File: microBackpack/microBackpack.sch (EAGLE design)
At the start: 93 parts, among them IC1 LM324D, IC2 LM324D, J2 USB_B_PTH, J4 2X6 FEMALE, U1 ATMEGA328P_TQFP, U10 TLP185, U11 TLP185, U2 5VREG-HS, U3 CP2102N-QFN24, U4 TVS_DIODE_4PK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

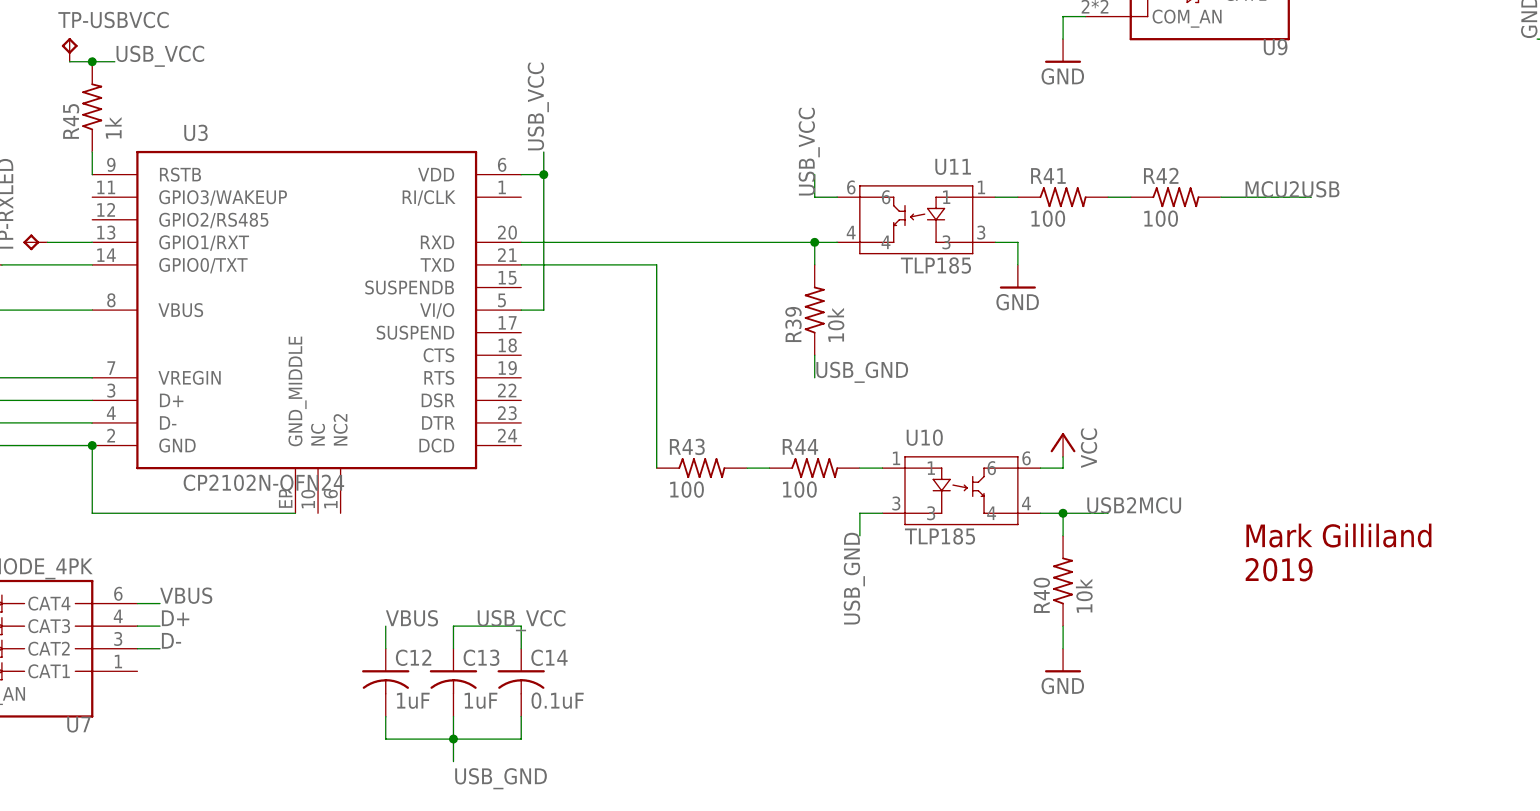
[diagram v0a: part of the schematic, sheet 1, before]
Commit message: Routed more traces
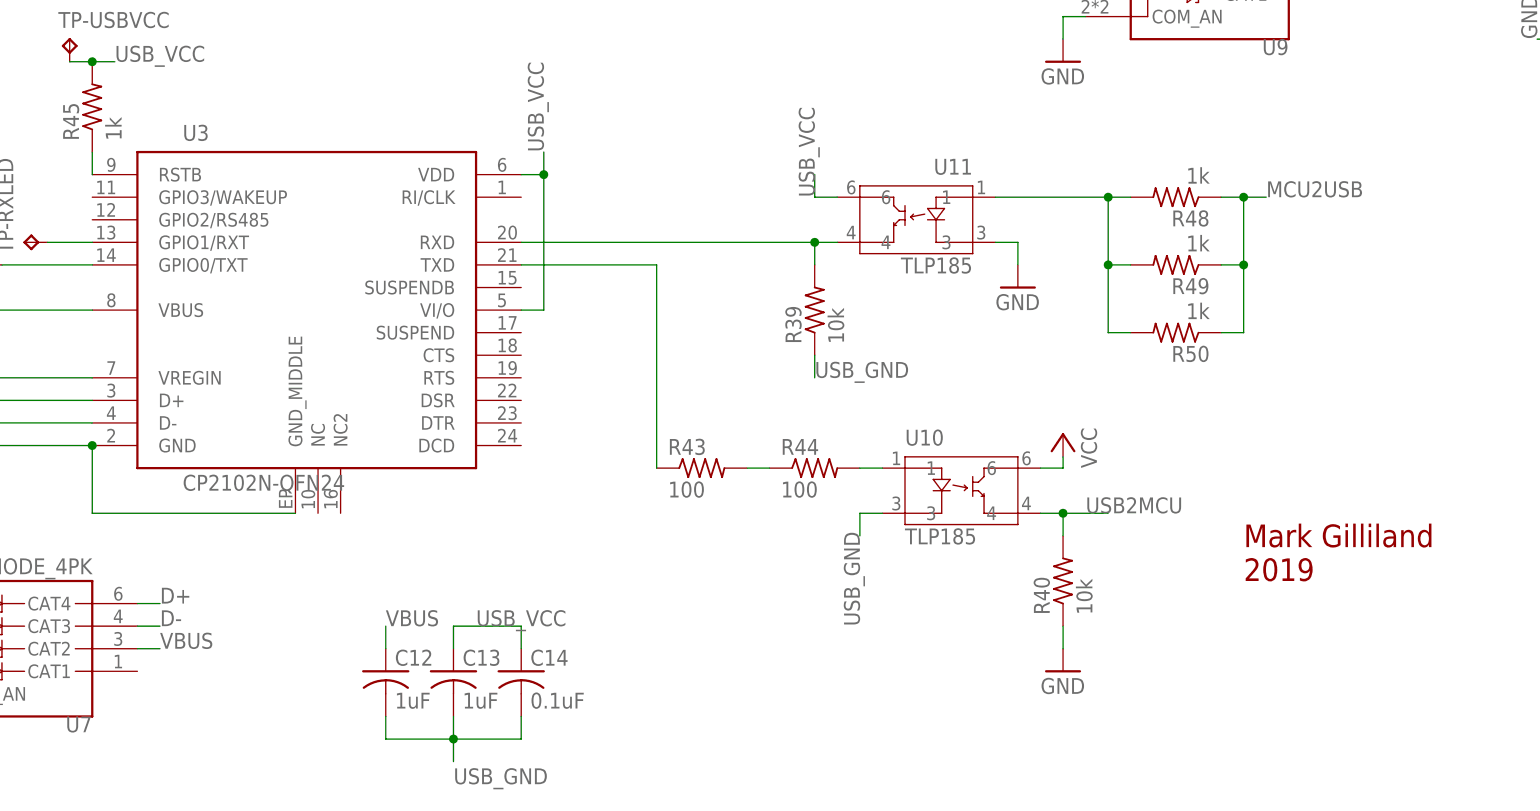
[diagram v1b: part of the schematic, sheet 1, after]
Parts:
- removed R41, R42: 100, rcl:R-US_R0603
- added R48, R49, R50: 1k, rcl:R-US_R0805
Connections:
- removed net N$13: R41.2, R42.1
- net D+: now also U7.CAT4; no longer U7.CAT3
- net D-: now also U7.CAT3; no longer U7.CAT2
- net MCU2USB: now also R48.1, R49.1, R50.1; no longer R42.2
- net N$5: now also R48.2, R49.2, R50.2; no longer R41.1
- net VBUS: now also U7.CAT2; no longer U7.CAT4
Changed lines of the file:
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@@
 <part name="P+8" library="supply1" library_urn="urn:adsk.eagle:library:371" deviceset="VCC" device=""/>
 <part name="GND23" library="supply1" library_urn="urn:adsk.eagle:library:371" deviceset="GND" device=""/>
-<part name="R41" library="rcl" library_urn="urn:adsk.eagle:library:334" deviceset="R-US_" device="R0603" package3d_urn="urn:adsk.eagle:package:23555/3" value="100"/>
-<part name="R42" library="rcl" library_urn="urn:adsk.eagle:library:334" deviceset="R-US_" device="R0603" package3d_urn="urn:adsk.eagle:package:23555/3" value="100"/>
 <part name="R43" library="rcl" library_urn="urn:adsk.eagle:library:334" deviceset="R-US_" device="R0603" package3d_urn="urn:adsk.eagle:package:23555/3" value="100"/>
 <part name="R44" library="rcl" library_urn="urn:adsk.eagle:library:334" deviceset="R-US_" device="R0603" package3d_urn="urn:adsk.eagle:package:23555/3" value="100"/>
@@
 <part name="C14" library="rcl" library_urn="urn:adsk.eagle:library:334" deviceset="C-US" device="C0805" package3d_urn="urn:adsk.eagle:package:23617/2" value="0.1uF"/>
 <part name="GND24" library="supply1" library_urn="urn:adsk.eagle:library:371" deviceset="GND" device=""/>
+<part name="R48" library="rcl" library_urn="urn:adsk.eagle:library:334" deviceset="R-US_" device="R0805" package3d_urn="urn:adsk.eagle:package:23553/2" value="1k"/>
+<part name="R49" library="rcl" library_urn="urn:adsk.eagle:library:334" deviceset="R-US_" device="R0805" package3d_urn="urn:adsk.eagle:package:23553/2" value="1k"/>
+<part name="R50" library="rcl" library_urn="urn:adsk.eagle:library:334" deviceset="R-US_" device="R0805" package3d_urn="urn:adsk.eagle:package:23553/2" value="1k"/>
 </parts>
 <sheets>
@@
 <attribute name="VALUE" x="154.94" y="12.7" size="1.778" layer="96"/>
 </instance>
-<instance part="R41" gate="G$1" x="157.48" y="68.58" smashed="yes">
-<attribute name="NAME" x="153.67" y="70.0786" size="1.778" layer="95"/>
-<attribute name="VALUE" x="153.67" y="65.278" size="1.778" layer="96"/>
-</instance>
-<instance part="R42" gate="G$1" x="170.18" y="68.58" smashed="yes">
-<attribute name="NAME" x="166.37" y="70.0786" size="1.778" layer="95"/>
-<attribute name="VALUE" x="166.37" y="65.278" size="1.778" layer="96"/>
-</instance>
 <instance part="R43" gate="G$1" x="116.84" y="38.1" smashed="yes">
 <attribute name="NAME" x="113.03" y="39.5986" size="1.778" layer="95"/>
@@
 <instance part="GND24" gate="1" x="152.4" y="58.42" smashed="yes">
 <attribute name="VALUE" x="149.86" y="55.88" size="1.778" layer="96"/>
+</instance>
+<instance part="R48" gate="G$1" x="170.18" y="68.58" smashed="yes" rot="R180">
+<attribute name="NAME" x="173.99" y="67.0814" size="1.778" layer="95" rot="R180"/>
+<attribute name="VALUE" x="173.99" y="71.882" size="1.778" layer="96" rot="R180"/>
+</instance>
+<instance part="R49" gate="G$1" x="170.18" y="60.96" smashed="yes" rot="R180">
+<attribute name="NAME" x="173.99" y="59.4614" size="1.778" layer="95" rot="R180"/>
+<attribute name="VALUE" x="173.99" y="64.262" size="1.778" layer="96" rot="R180"/>
+</instance>
+<instance part="R50" gate="G$1" x="170.18" y="53.34" smashed="yes" rot="R180">
+<attribute name="NAME" x="173.99" y="51.8414" size="1.778" layer="95" rot="R180"/>
+<attribute name="VALUE" x="173.99" y="56.642" size="1.778" layer="96" rot="R180"/>
 </instance>
 </instances>
@@
 </segment>
 <segment>
-<wire x1="175.26" y1="68.58" x2="185.42" y2="68.58" width="0.1524" layer="91"/>
-<label x="177.8" y="68.58" size="1.778" layer="95"/>
-<pinref part="R42" gate="G$1" pin="2"/>
+<pinref part="R48" gate="G$1" pin="1"/>
+<wire x1="175.26" y1="68.58" x2="177.8" y2="68.58" width="0.1524" layer="91"/>
+<wire x1="177.8" y1="68.58" x2="177.8" y2="60.96" width="0.1524" layer="91"/>
+<pinref part="R49" gate="G$1" pin="1"/>
+<wire x1="177.8" y1="60.96" x2="175.26" y2="60.96" width="0.1524" layer="91"/>
+<wire x1="177.8" y1="68.58" x2="180.34" y2="68.58" width="0.1524" layer="91"/>
+<junction x="177.8" y="68.58"/>
+<label x="180.34" y="68.58" size="1.778" layer="95"/>
+<pinref part="R50" gate="G$1" pin="1"/>
+<wire x1="175.26" y1="53.34" x2="177.8" y2="53.34" width="0.1524" layer="91"/>
+<wire x1="177.8" y1="60.96" x2="177.8" y2="53.34" width="0.1524" layer="91"/>
+<junction x="177.8" y="60.96"/>
 </segment>
 </net>
@@
 </segment>
 </net>
-<net name="N$13" class="0">
-<segment>
-<pinref part="R41" gate="G$1" pin="2"/>
-<pinref part="R42" gate="G$1" pin="1"/>
-<wire x1="162.56" y1="68.58" x2="165.1" y2="68.58" width="0.1524" layer="91"/>
-</segment>
-</net>
 <net name="N$17" class="0">
 <segment>
@@
 </net>
 <net name="D-" class="0">
-<segment>
-<pinref part="U7" gate="G$1" pin="CAT2"/>
-<wire x1="53.34" y1="17.78" x2="55.88" y2="17.78" width="0.1524" layer="91"/>
-<label x="55.88" y="17.78" size="1.778" layer="95"/>
-</segment>
 <segment>
 <pinref part="J2" gate="G$1" pin="D-"/>
@@
 <label x="22.86" y="45.72" size="1.778" layer="95"/>
 </segment>
-</net>
-<net name="D+" class="0">
 <segment>
 <pinref part="U7" gate="G$1" pin="CAT3"/>
@@
 <label x="55.88" y="20.32" size="1.778" layer="95"/>
 </segment>
+</net>
+<net name="D+" class="0">
 <segment>
 <pinref part="U3" gate="G$1" pin="D+"/>
@@
 <label x="22.86" y="43.18" size="1.778" layer="95"/>
 </segment>
-</net>
-<net name="VBUS" class="0">
 <segment>
 <pinref part="U7" gate="G$1" pin="CAT4"/>
@@
 <label x="55.88" y="22.86" size="1.778" layer="95"/>
 </segment>
+</net>
+<net name="VBUS" class="0">
 <segment>
 <pinref part="J2" gate="G$1" pin="VBUS"/>
@@
 <wire x1="81.28" y1="17.78" x2="81.28" y2="20.32" width="0.1524" layer="91"/>
 <label x="81.28" y="20.32" size="1.778" layer="95"/>
+</segment>
+<segment>
+<pinref part="U7" gate="G$1" pin="CAT2"/>
+<wire x1="53.34" y1="17.78" x2="55.88" y2="17.78" width="0.1524" layer="91"/>
+<label x="55.88" y="17.78" size="1.778" layer="95"/>
 </segment>
 </net>
@@
 <net name="N$5" class="0">
 <segment>
-<pinref part="R41" gate="G$1" pin="1"/>
+<pinref part="R48" gate="G$1" pin="2"/>
+<wire x1="165.1" y1="68.58" x2="162.56" y2="68.58" width="0.1524" layer="91"/>
+<wire x1="162.56" y1="68.58" x2="162.56" y2="60.96" width="0.1524" layer="91"/>
+<pinref part="R49" gate="G$1" pin="2"/>
+<wire x1="162.56" y1="60.96" x2="165.1" y2="60.96" width="0.1524" layer="91"/>
+<junction x="162.56" y="68.58"/>
 <pinref part="U11" gate="U$1" pin="1"/>
-<wire x1="152.4" y1="68.58" x2="149.86" y2="68.58" width="0.1524" layer="91"/>
-</segment>
-</net>
+<wire x1="162.56" y1="68.58" x2="149.86" y2="68.58" width="0.1524" layer="91"/>
+<wire x1="162.56" y1="60.96" x2="162.56" y2="53.34" width="0.1524" layer="91"/>
+<junction x="162.56" y="60.96"/>
+<pinref part="R50" gate="G$1" pin="2"/>
+<wire x1="162.56" y1="53.34" x2="165.1" y2="53.34" width="0.1524" layer="91"/>
+</segment>
+</net>

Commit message: Moved headers and holes
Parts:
- added H6: MOUNT-HOLE2.8, holes:MOUNT-HOLE2.8
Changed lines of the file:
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@@
 <?xml version="1.0" encoding="utf-8"?>
 <!DOCTYPE eagle SYSTEM "eagle.dtd">
-<eagle version="9.4.2">
+<eagle version="9.1.2">
 <drawing>
 <settings>
@@
 <part name="R49" library="rcl" library_urn="urn:adsk.eagle:library:334" deviceset="R-US_" device="R0805" package3d_urn="urn:adsk.eagle:package:23553/2" value="1k"/>
 <part name="R50" library="rcl" library_urn="urn:adsk.eagle:library:334" deviceset="R-US_" device="R0805" package3d_urn="urn:adsk.eagle:package:23553/2" value="1k"/>
+<part name="H6" library="holes" library_urn="urn:adsk.eagle:library:237" deviceset="MOUNT-HOLE" device="2.8" package3d_urn="urn:adsk.eagle:package:14271/1"/>
 </parts>
 <sheets>
@@
 <attribute name="VALUE" x="173.99" y="56.642" size="1.778" layer="96" rot="R180"/>
 </instance>
+<instance part="H6" gate="G$1" x="246.38" y="40.64" smashed="yes">
+<attribute name="NAME" x="248.412" y="41.2242" size="1.778" layer="95"/>
+<attribute name="VALUE" x="248.412" y="38.1762" size="1.778" layer="96"/>
+</instance>
 </instances>

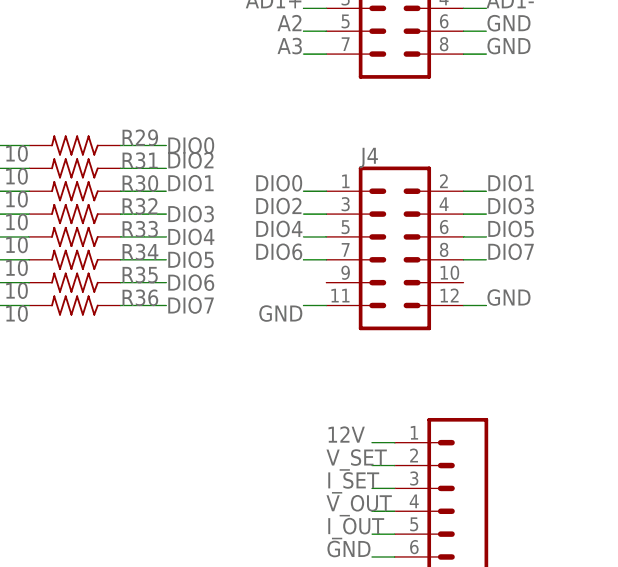
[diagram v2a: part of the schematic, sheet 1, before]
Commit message: Full layout complete. Added 9V to DIO header
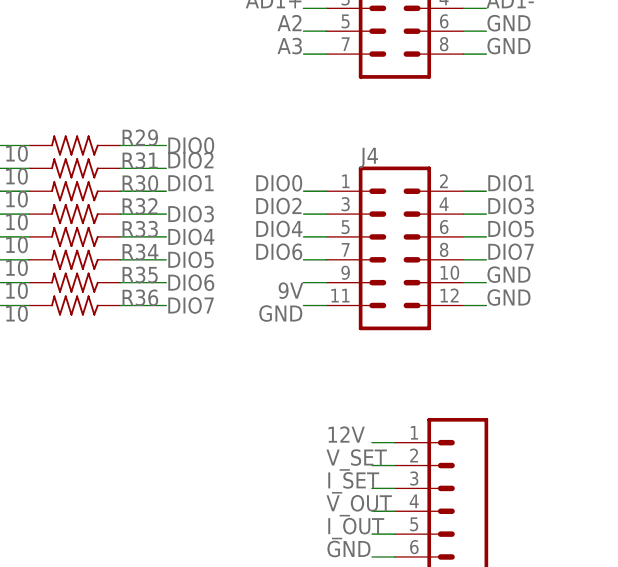
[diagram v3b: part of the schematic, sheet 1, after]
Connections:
- net 9V: now also J4.9
- net GND: now also J4.10
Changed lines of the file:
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@@
 <?xml version="1.0" encoding="utf-8"?>
 <!DOCTYPE eagle SYSTEM "eagle.dtd">
-<eagle version="9.1.2">
+<eagle version="9.4.2">
 <drawing>
 <settings>
@@
 <pinref part="GND24" gate="1" pin="GND"/>
 </segment>
+<segment>
+<pinref part="J4" gate="G$1" pin="10"/>
+<wire x1="256.54" y1="127" x2="259.08" y2="127" width="0.1524" layer="91"/>
+<label x="259.08" y="127" size="1.778" layer="95"/>
+</segment>
 </net>
 <net name="MISO" class="0">
@@
 <junction x="121.92" y="198.12"/>
 </segment>
-</net>
+<segment>
+<pinref part="J4" gate="G$1" pin="9"/>
+<wire x1="241.3" y1="127" x2="238.76" y2="127" width="0.1524" layer="91"/>
+<label x="238.76" y="127" size="1.778" layer="95" rot="R180"/>
+</segment>
+</net>

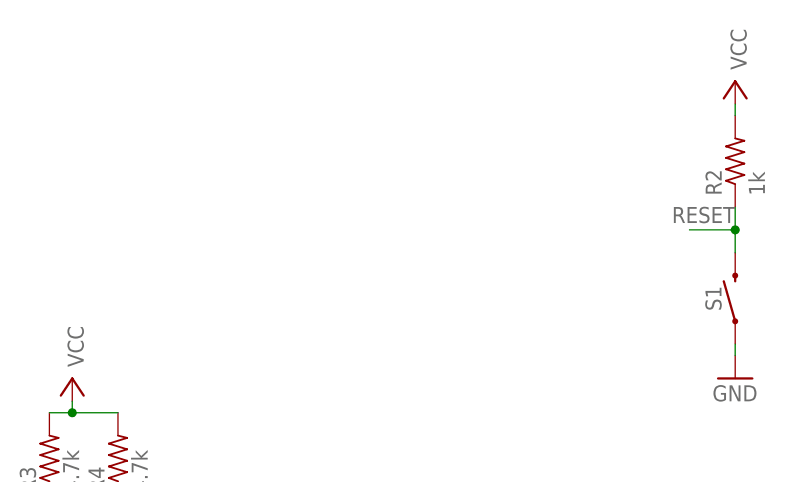
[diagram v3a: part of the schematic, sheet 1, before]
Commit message: Added test points and labels
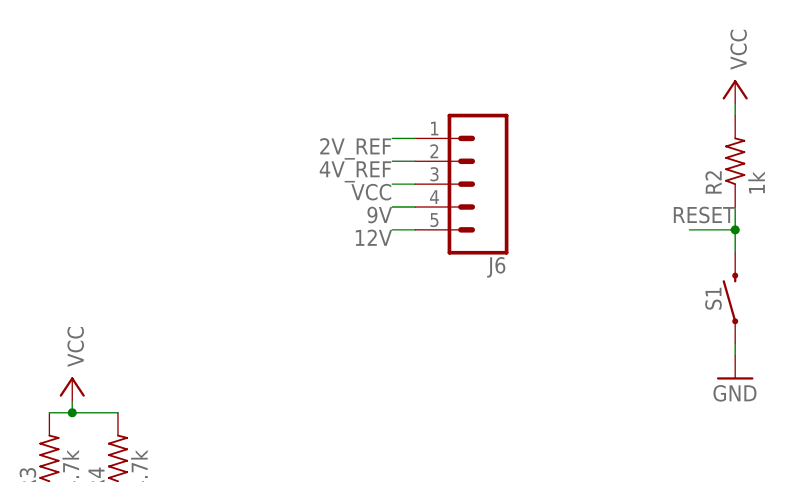
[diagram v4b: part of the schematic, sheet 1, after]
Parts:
- added J6: (no value), SparkFun-Connectors:CONN_05NO_SILK
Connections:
- net 12V: now also J6.5
- net 2V_REF: now also J6.1
- net 4V_REF: now also J6.2
- net 9V: now also J6.4
- net VCC: now also J6.3
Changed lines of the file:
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@@
 <part name="R50" library="rcl" library_urn="urn:adsk.eagle:library:334" deviceset="R-US_" device="R0805" package3d_urn="urn:adsk.eagle:package:23553/2" value="1k"/>
 <part name="H6" library="holes" library_urn="urn:adsk.eagle:library:237" deviceset="MOUNT-HOLE" device="2.8" package3d_urn="urn:adsk.eagle:package:14271/1"/>
+<part name="J6" library="SparkFun-Connectors" library_urn="urn:adsk.eagle:library:513" deviceset="CONN_05" device="NO_SILK" package3d_urn="urn:adsk.eagle:package:38108/1"/>
 </parts>
 <sheets>
@@
 <attribute name="VALUE" x="248.412" y="38.1762" size="1.778" layer="96"/>
 </instance>
+<instance part="J6" gate="G$1" x="190.5" y="193.04" smashed="yes" rot="R180">
+<attribute name="VALUE" x="193.04" y="202.946" size="1.778" layer="96" font="vector" rot="R180"/>
+<attribute name="NAME" x="193.04" y="184.912" size="1.778" layer="95" font="vector" rot="R180"/>
+</instance>
 </instances>
 <busses>
@@
 <wire x1="157.48" y1="39.37" x2="157.48" y2="38.1" width="0.1524" layer="91"/>
 </segment>
+<segment>
+<pinref part="J6" gate="G$1" pin="3"/>
+<wire x1="182.88" y1="193.04" x2="180.34" y2="193.04" width="0.1524" layer="91"/>
+<label x="180.34" y="193.04" size="1.778" layer="95" rot="R180"/>
+</segment>
 </net>
 <net name="12V" class="0">
@@
 <wire x1="91.44" y1="198.12" x2="91.44" y2="195.58" width="0.1524" layer="91"/>
 <junction x="91.44" y="198.12"/>
+</segment>
+<segment>
+<pinref part="J6" gate="G$1" pin="5"/>
+<wire x1="182.88" y1="187.96" x2="180.34" y2="187.96" width="0.1524" layer="91"/>
+<label x="180.34" y="187.96" size="1.778" layer="95" rot="R180"/>
 </segment>
 </net>
@@
 <wire x1="38.1" y1="149.86" x2="38.1" y2="152.4" width="0.1524" layer="91"/>
 <junction x="38.1" y="152.4"/>
+</segment>
+<segment>
+<pinref part="J6" gate="G$1" pin="2"/>
+<wire x1="182.88" y1="195.58" x2="180.34" y2="195.58" width="0.1524" layer="91"/>
+<label x="180.34" y="195.58" size="1.778" layer="95" rot="R180"/>
 </segment>
 </net>
@@
 <label x="238.76" y="127" size="1.778" layer="95" rot="R180"/>
 </segment>
+<segment>
+<pinref part="J6" gate="G$1" pin="4"/>
+<wire x1="182.88" y1="190.5" x2="180.34" y2="190.5" width="0.1524" layer="91"/>
+<label x="180.34" y="190.5" size="1.778" layer="95" rot="R180"/>
+</segment>
 </net>
 <net name="FGEN" class="0">
@@
 </segment>
 </net>
+<net name="2V_REF" class="0">
+<segment>
+<pinref part="J6" gate="G$1" pin="1"/>
+<wire x1="182.88" y1="198.12" x2="180.34" y2="198.12" width="0.1524" layer="91"/>
+<label x="180.34" y="198.12" size="1.778" layer="95" rot="R180"/>
+</segment>
+</net>

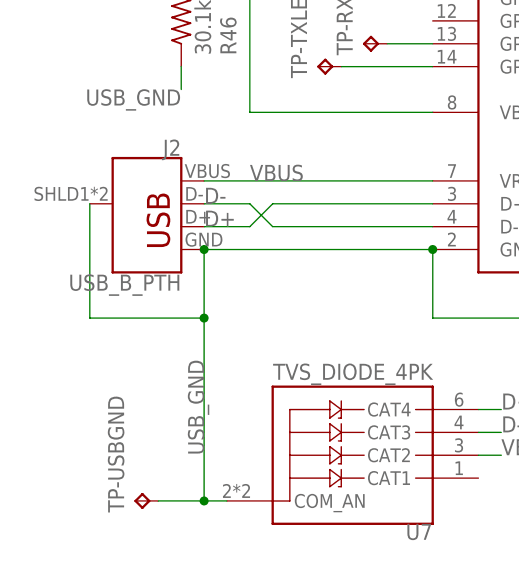
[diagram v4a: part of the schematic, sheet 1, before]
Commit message: Added vertical USB. Ready to purchase
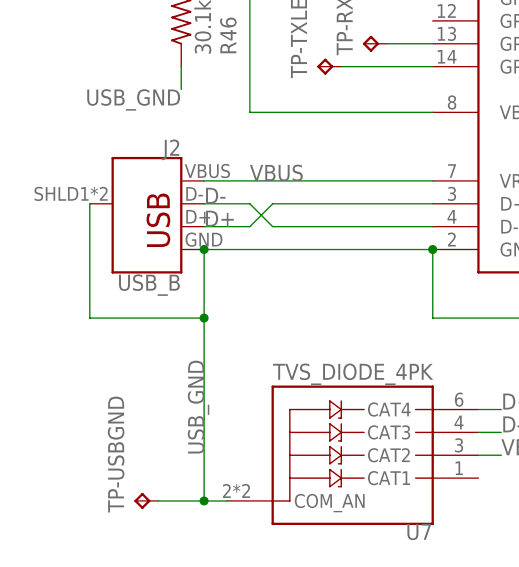
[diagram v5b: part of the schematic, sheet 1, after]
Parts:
- J2: value USB_B_PTH -> USB_B; device SparkFun-Connectors:USB_B_PTH -> microBackpackLib:USB_B
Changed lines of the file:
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@@
 <?xml version="1.0" encoding="utf-8"?>
 <!DOCTYPE eagle SYSTEM "eagle.dtd">
-<eagle version="9.4.2">
+<eagle version="9.1.2">
 <drawing>
 <settings>
@@
 <part name="GND7" library="supply1" library_urn="urn:adsk.eagle:library:371" deviceset="GND" device=""/>
 <part name="P+5" library="supply1" library_urn="urn:adsk.eagle:library:371" deviceset="VCC" device=""/>
-<part name="J2" library="SparkFun-Connectors" library_urn="urn:adsk.eagle:library:513" deviceset="USB_B" device="_PTH" package3d_urn="urn:adsk.eagle:package:38301/1"/>
+<part name="J2" library="microBackpackLib" deviceset="USB_B" device=""/>
 <part name="J3" library="SparkFun-Connectors" library_urn="urn:adsk.eagle:library:513" deviceset="CONN_04X2" device="" package3d_urn="urn:adsk.eagle:package:38103/1"/>
 <part name="J4" library="SparkFun-Connectors" library_urn="urn:adsk.eagle:library:513" deviceset="CONN_06X2" device="PTH_FEMALE" package3d_urn="urn:adsk.eagle:package:38277/1" value="2X6 FEMALE"/>
